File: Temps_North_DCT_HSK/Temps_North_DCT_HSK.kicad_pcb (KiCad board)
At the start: 2 copper layers, 53.3 x 63.5 mm, 9 parts, among them J1 North_Temps_1, J2 North_Temps_2, J3 Internal_Temps_DCT_HSK_Box_1, J4 Internal_Temps_DCT_HSK_Box_2

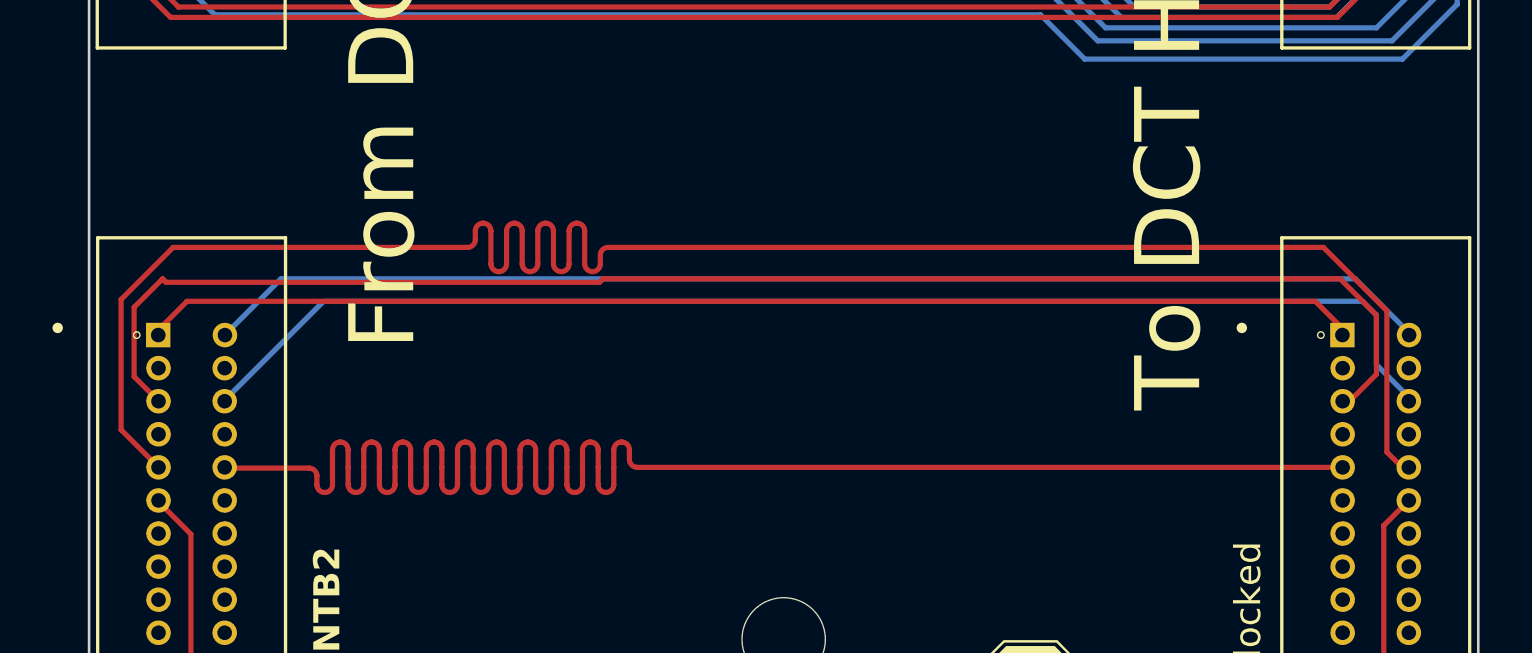
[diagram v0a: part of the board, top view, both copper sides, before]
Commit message: Tuned RTD tracks for Temp boards
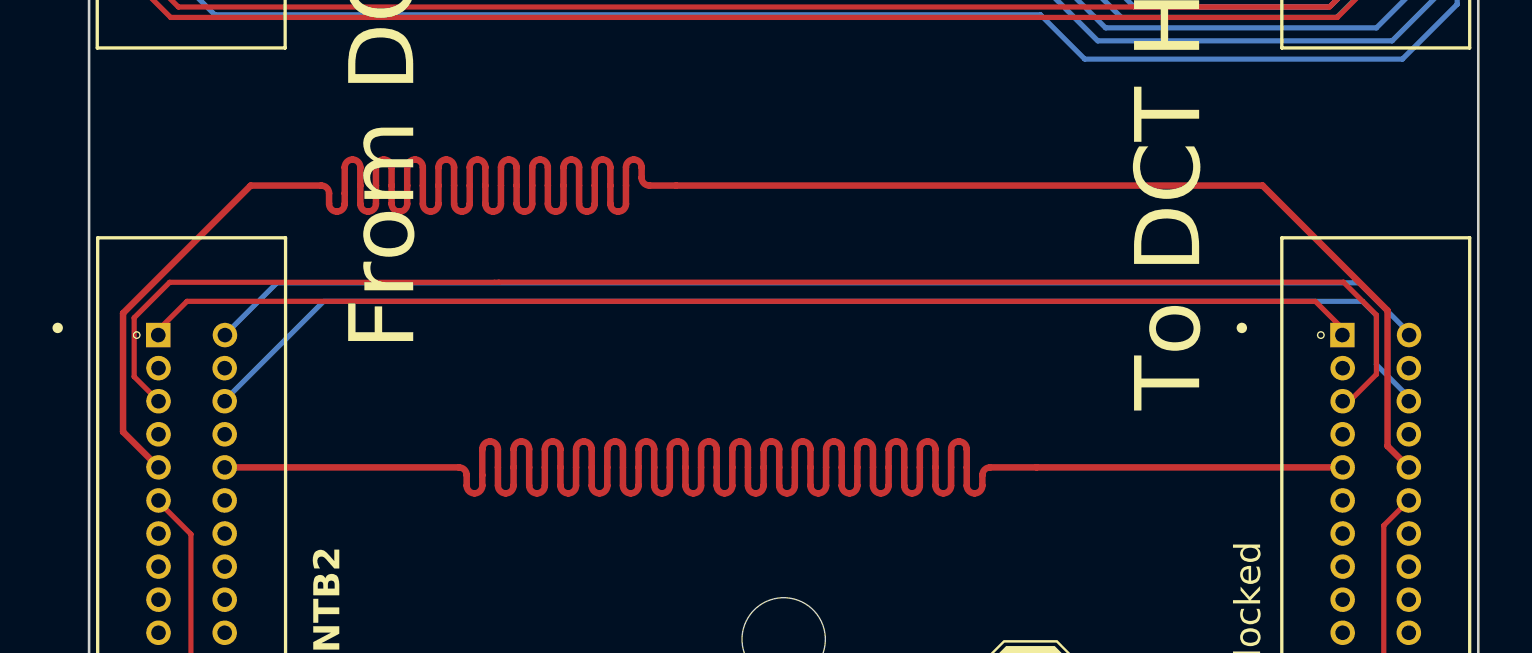
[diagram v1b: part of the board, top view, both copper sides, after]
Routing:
- net /TD2_10: track 75.7 -> 99.2 mm
- net /TD2_9: track 76.6 -> 99.5 mm

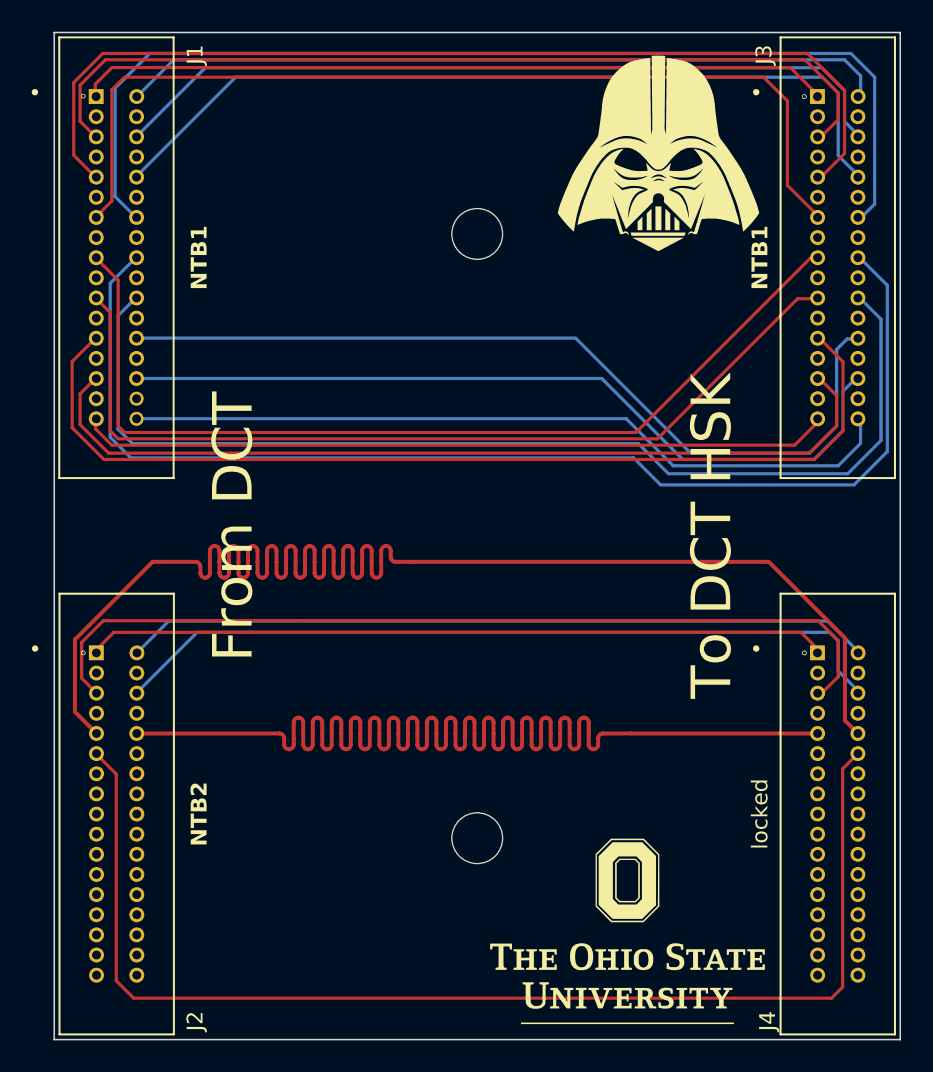
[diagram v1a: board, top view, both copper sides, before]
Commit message: Tuned RTD tracks on Temp boards
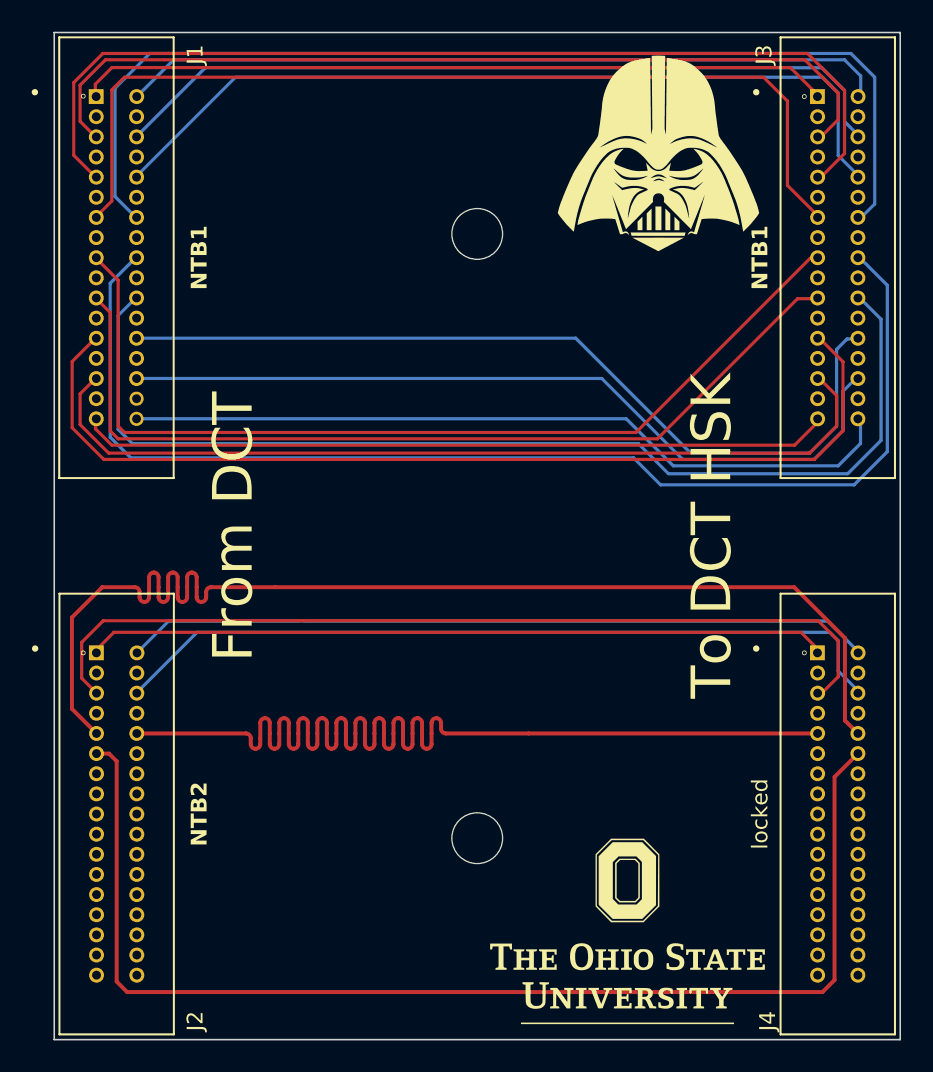
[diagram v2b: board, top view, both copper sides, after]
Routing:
- net /TD2_10: track 99.2 -> 75.6 mm
- net /TD2_9: track 99.5 -> 75.9 mm
- net /TD2_11: track 76.7 -> 76.1 mm
